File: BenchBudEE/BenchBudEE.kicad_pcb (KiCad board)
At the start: 4 copper layers, 165.1 x 63.5 mm, 106 parts, among them K1 1461069-5, P1 24 Pin MiniFit JR, P2 CONN_3X2, P3 CONN_2, P4 12 Pin Terminal Block, P5 3 Pin TB, Q1 2N3904, Q2 DMN65D8L-7, Q3 AOD476, Q4 AOD476, SW1 Power Switch, U1 LTV-816S, U10 MCP4801, U2 MCP3901, U3 LMT84, U4 OPA4170, U6 LM317, U7 LM337T, U8 LM337T, U9 LM317

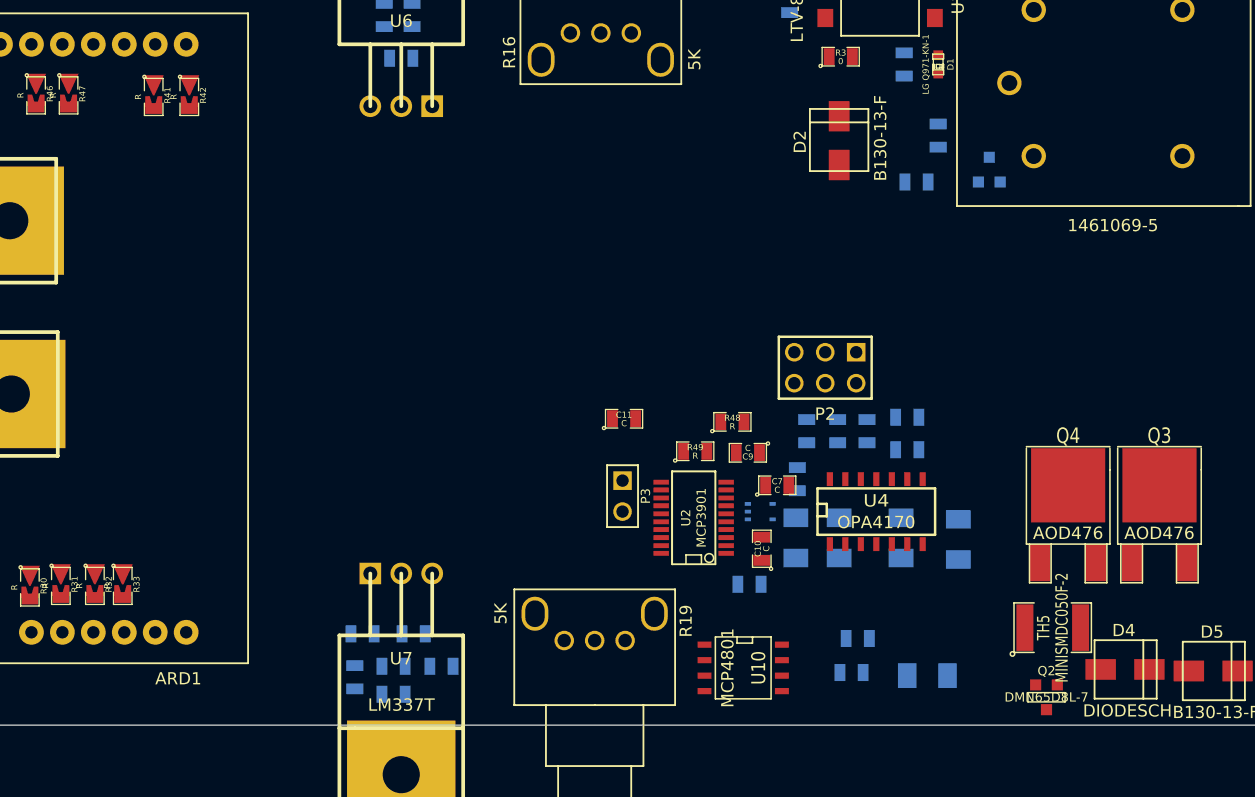
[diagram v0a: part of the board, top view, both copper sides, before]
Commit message: Roughly placed the LED Driver module components.
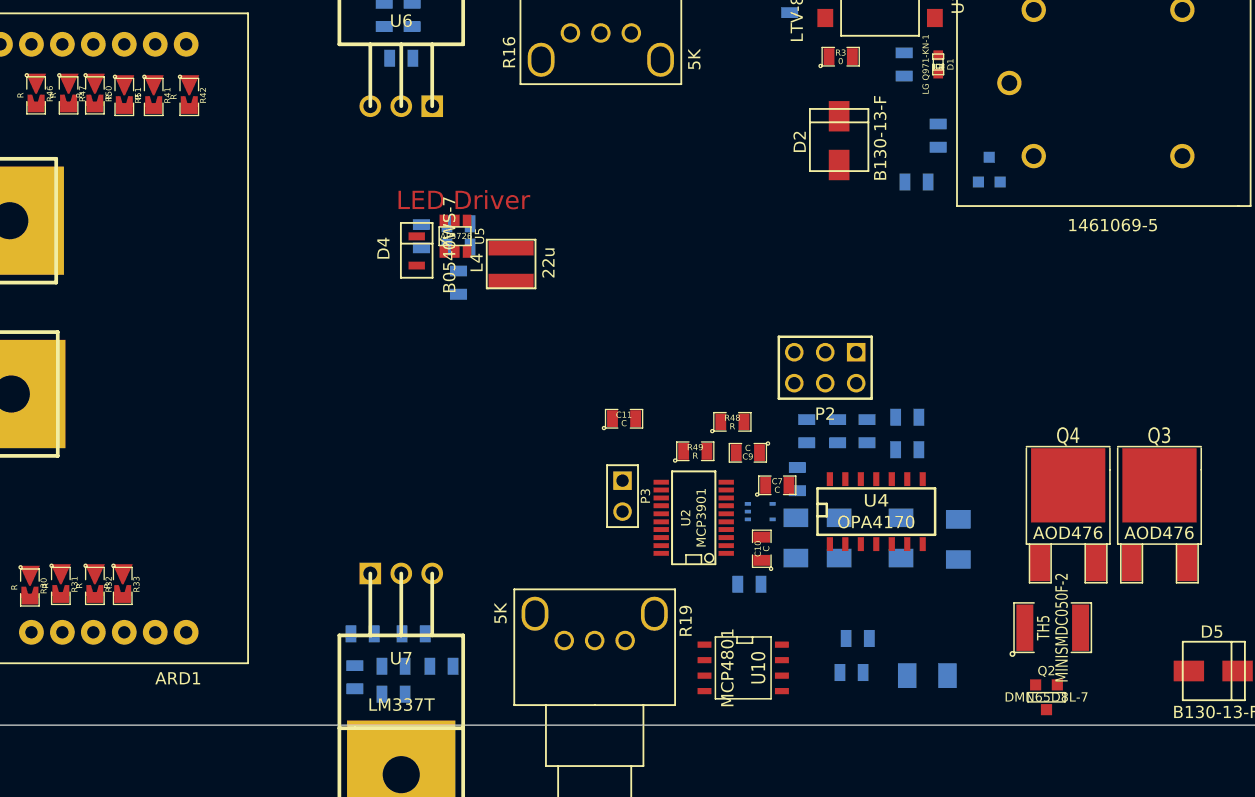
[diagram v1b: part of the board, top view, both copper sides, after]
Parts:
- added C12: C, SM0805, B.Cu at (166.6, 136.4)
- added C4: 1u, SM0805, B.Cu at (169.7, 140.2)
- added C5: 1u, SM0805, B.Cu at (169.7, 135.4)
- added L4: 22u, NR4012, F.Cu at (174.0, 138.7)
- added R15: 15, SM0805, B.Cu at (169.7, 137.3)
- added R50: R, SM0805-blob, F.Cu at (139.8, 124.8)
- added R51: R, SM0805-blob, F.Cu at (142.2, 125.0)
- added U5: AP5726, SOT23_6, F.Cu at (169.4, 136.4)
- D4: value DIODESCH -> B0540WS-7; footprint SMA -> SOD-323
- moved D4 65.2 mm to (166.2, 138.8), turned to 90 degrees
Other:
- board text added: "LED Driver"
